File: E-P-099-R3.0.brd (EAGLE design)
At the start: 113.1 x 96.5 mm, 103 parts, among them J1 AVR_ISP, Q1 BSS101, Q2 BSS101, Q3 BSS101, Q4 BSS101, Q5 BSS101, Q6 BSS101

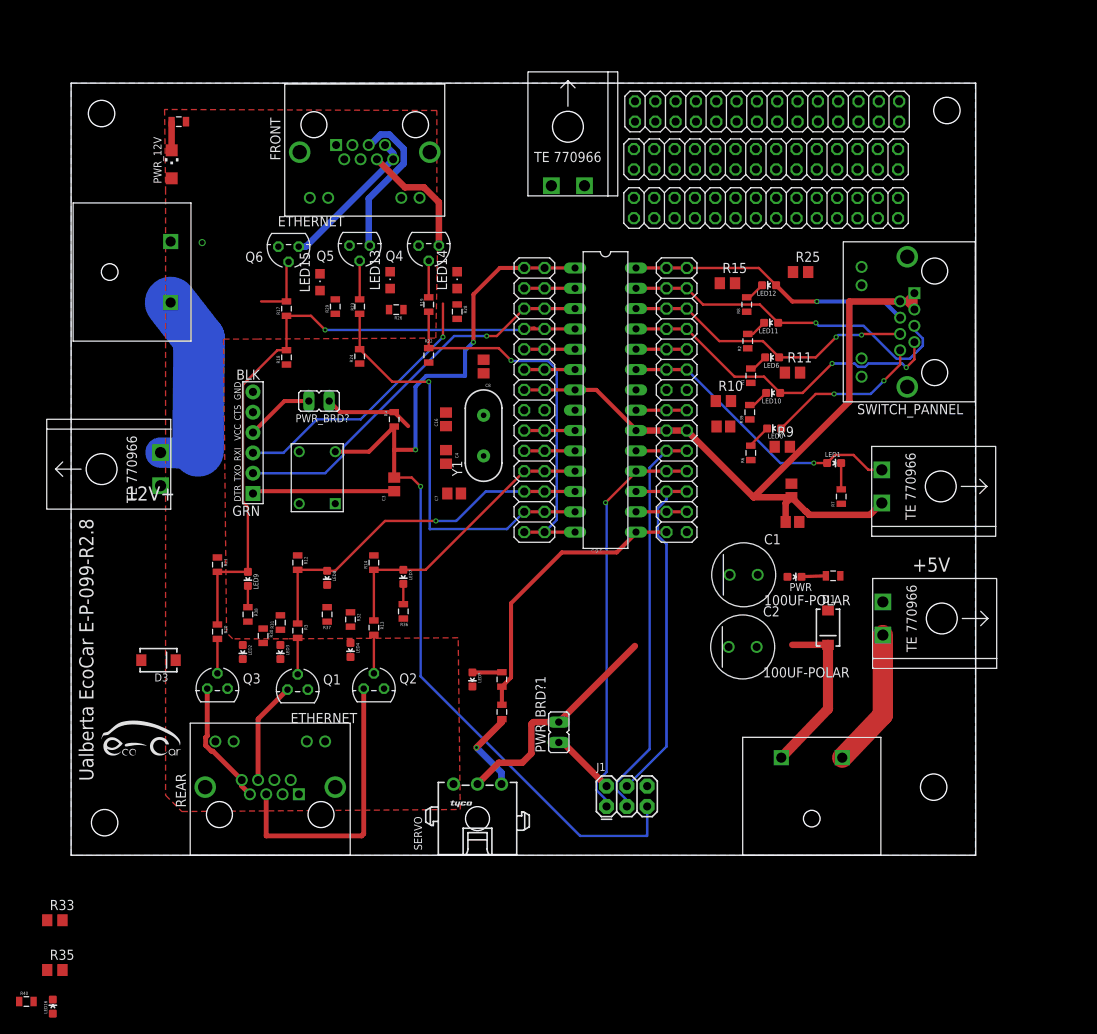
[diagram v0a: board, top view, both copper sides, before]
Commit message: added separate power for servo, cleaned up a bit of board layout, remade some missing eagle libraries and added them to library repo
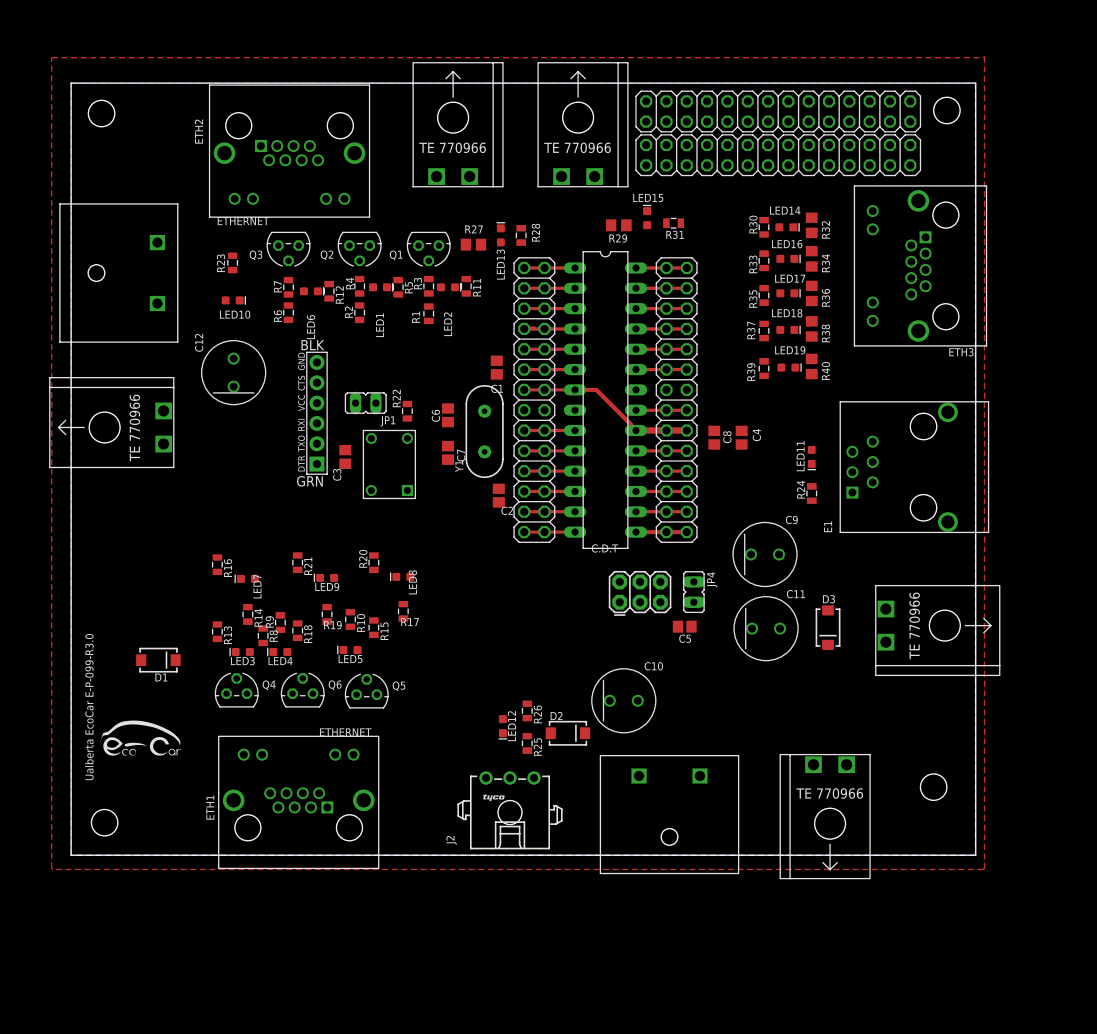
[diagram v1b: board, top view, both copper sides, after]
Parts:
- removed C14, C15, C16: 10uF, adafruit:C0805
- removed FRONT, REAR, SWITCH_PANNEL: ETHERNET, ETHERNET-3:A122645-ND
- removed LED0, PWR: (no value), SparkFun-LED:LED-0603
- removed PWR_12V: (no value), E14-P-099-R21.2(US_drills):CHIPLED_1206
- removed PWR_BRD?, PWR_BRD?1: (no value), E-P-099-R2.2:JP1
- removed SERVO: 1445055-3, con-amp:1445055-3
- removed U$1, U$3, U$5, U$8: TE770966, Shell2013(1):2X1-MATE-N-LOCK
- removed U$12: PUSH_BUTTON, E-P-099-R2.2:PUSHBUTTON
- removed U$2, U$9: FUSEMINI-BLADE, Shell2013:MINI-BLADE-FUSE
- removed U$4: ATMEGA328, E-P-099-R2.2:DIP28-0.3IN
- added AT1: ATMEGA328, atmega328p:DIP28-0.3IN
- added B1: PUSH_BUTTON, PushButton:PUSHBUTTON
- added C10, C11, C12, C9: 100UF-POLAR, 100uF_Cap:EEU-FR1H101
- added C6: 10uF, adafruit:C0805
- added D2: MBRA140, SparkFun-DiscreteSemi:SMA-DIODE
- added E1: 5555140-6, 5555140-6 RJ11:1734723-1_RJ11
- added ETH1, ETH2, ETH3: ETHERNET, ETHERNET-3:A122645-ND
- added J2: 1445055-3, con-amp:1445055-3
- added JP1: (no value), E-P-099-R2.2:JP1
- added LED17, LED18, LED19: (no value), SparkFun-LED:LED-0603
- added TE1, TE3: FUSEMINI-BLADE, Fuse:MINI-BLADE-FUSE
- added TE2, TE5, TE6, TE7: TE770966, TwoPinWhiteTEConnector:2X1-MATE-N-LOCK
- added TE4: SERVO_PWR, TwoPinWhiteTEConnector:2X1-MATE-N-LOCK
- C1, C2: value 100UF-POLAR -> 20pF; device 100uF_Cap:EEU-FR1H101 -> adafruit:C0805
- C4, C5: value 0.1uF -> 10uF
- C7, C8: value 20pF -> 0.1uF
- JP2: value (none) -> FTDI_DEVICE; device E-P-099-R2.2:2X14 -> SparkFun-Connectors:FTDI_DEVICE_SIDE
- JP4: device E-P-099-R2.2:2X14 -> E-P-099-R2.2:JP1
- JP6: value FTDI_DEVICE -> (none); device SparkFun-Connectors:FTDI_DEVICE_SIDE -> E-P-099-R2.2:2X14
- LED13, LED14, LED15: device led:CHIPLED_0805 -> SparkFun-LED:LED-0603
- R1, R2, R6: value 1K -> 10k
- R10, R9: value 10K -> 430; device resistor:R0805 -> SparkFun-Passives:0805
- R11, R33, R35: value 10K -> 1K; device resistor:R0805 -> SparkFun-Passives:0805
- R12, R22, R24: value 10k -> 1K
- R14: value 10k -> 430
- R15, R25: value 10K -> 100; device resistor:R0805 -> SparkFun-Passives:0805
- R16: value 1k -> 10k
- R17, R19: value 100 -> 430
- R18: value 10k -> 100
- R20: value 100 -> 10k
- R23: value 100 -> 1k
- R26, R8: value 1K -> 430
- R27: value 100 -> 10K; device SparkFun-Passives:0805 -> resistor:R0805
- R29, R40: value 1K -> 10K; device SparkFun-Passives:0805 -> resistor:R0805
- R30, R31, R37: value 430 -> 1K
- R32, R34, R36, R38: value 430 -> 10K; device SparkFun-Passives:0805 -> resistor:R0805
- R4, R7: value 1K -> 100
- moved LED16 131.0 mm to (78.1, 69.5)
- moved R40 126.2 mm to (81.2, 56.0), turned to 270 degrees
- moved R35 122.3 mm to (75.2, 64.9), turned to 270 degrees
- moved R33 121.0 mm to (75.2, 69.2), turned to 270 degrees
- moved D1 83.8 mm to (-0.51, 19.3), turned to 0 degrees
- moved D3 83.8 mm to (83.2, 23.4), turned to 270 degrees
- moved R30 80.8 mm to (75.2, 73.4), turned to 90 degrees
- moved R38 79.0 mm to (81.2, 60.7)
- moved JP6 77.6 mm to (77.0, 87.9), turned to 0 degrees
- moved R32 75.8 mm to (81.2, 73.7)
- moved R7 73.9 mm to (15.7, 65.9)
- moved R8 73.3 mm to (12.6, 22.4), turned to 270 degrees
- moved R31 70.0 mm to (63.9, 73.9), turned to 180 degrees
- moved LED10 68.5 mm to (8.76, 64.3), turned to 0 degrees
- moved R25 68.1 mm to (45.6, 8.89), turned to 270 degrees
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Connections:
- removed net N$24: C8.1, Y1.2
- new net N$29: TE3.IN, TE4.CIRCUIT1
- new net SERVO_V: C10.P, D2.C, J2.2, TE3.OUT
- net +12V: now also C12.P, D1.C, ETH1.P$1, ETH1.P$2, ETH1.P$3, ETH1.P$4, ETH2.P$1, ETH2.P$2, ETH2.P$3, ETH2.P$4, LED10.A, R10.1, R11.2, R12.1, R5.1, R8.1, R9.2, TE1.OUT; no longer D3.C, FRONT.P$1, FRONT.P$2, FRONT.P$3, FRONT.P$4, PWR_12V.A, R26.1, R28.2, R29.1, R30.1, R31.2, R32.1, REAR.P$1, REAR.P$2, REAR.P$3, REAR.P$4, U$9.OUT
- net +5V: now also AT1.20, AT1.7, C11.P, C6.1, C7.1, C8.1, C9.P, D3.C, ETH3.P$1, ETH3.P$2, ETH3.P$3, JP1.1, JP3.13, JP3.14, JP4.2, JP5.17, JP5.18, LED11.A, R22.2, TE5.CIRCUIT1, TE6.CIRCUIT1, TE7.CIRCUIT2; no longer C1.P, C14.1, C15.1, C16.1, C2.P, D1.C, JP3.17, JP3.18, JP4.13, JP4.14, PWR.A, PWR_BRD?.1, PWR_BRD?1.2, R4.2, SERVO.2, SWITCH_PANNEL.P$1, SWITCH_PANNEL.P$2, SWITCH_PANNEL.P$3, U$2.OUT, U$3.CIRCUIT1, U$4.20, U$4.7, U$5.CIRCUIT1
- net BLINK_L: now also AT1.13, JP3.25, JP3.26, R2.2, R4.2; no longer JP4.25, JP4.26, R23.2, R24.2, U$4.13
- net BLINK_R: now also AT1.14, JP3.27, JP3.28, R1.1, R3.2; no longer JP4.27, JP4.28, R19.2, R22.1, U$4.14
- net BREAK_SWITCH: now also AT1.23, JP5.11, JP5.12, LED13.A, R27.2, TE5.CIRCUIT2; no longer JP3.11, JP3.12, LED1.A, R35.2, U$3.CIRCUIT2, U$4.23
- net BRK_L_HIGH: now also AT1.12, JP3.23, JP3.24, LED9.A, R18.1, R21.2; no longer JP4.23, JP4.24, LED8.A, R12.2, R3.1, U$4.12
- net BRK_R_HIGH: now also AT1.11, JP3.21, JP3.22, LED8.A, R15.1, R20.1; no longer JP4.21, JP4.22, LED7.A, R13.1, R14.1, U$4.11
- net DRIVING_LIGHTS: now also AT1.4, JP3.7, JP3.8, LED7.A, R13.1, R16.2, R6.2, R7.1; no longer JP4.7, JP4.8, LED9.A, R17.1, R18.2, R20.1, R21.2, U$4.4
- net DRIVING_LIGHTS_SWITCH: now also AT1.26, ETH3.P$6, JP5.5, JP5.6, LED17.A, R36.2; no longer JP3.5, JP3.6, LED6.A, R11.2, SWITCH_PANNEL.P$6, U$4.26
- net DTR: now also JP2.P$1; no longer JP6.P$1
- net FREE: now also ETH3.P$8, LED19.A, R40.2; no longer LED0.A, R9.2, SWITCH_PANNEL.P$8
- net GND: now also AT1.22, AT1.8, B1.L1, C1.2, C10.G, C11.G, C12.G, C2.2, C6.2, C9.G, D2.A, E1.1, E1.6, E1.SH1, E1.SH2, ETH1.P$13, ETH1.P$14, J2.3, JP2.P$6, JP3.15, JP3.16, JP5.13, JP5.14, LED12.C, R1.2, R16.1, R17.2, R19.2, R20.2, R23.2, R27.1, R28.1, R29.2, R30.1, R31.1, R32.1, R33.1, R34.1, R36.1, R37.1, R38.1, TE2.CIRCUIT2, TE4.CIRCUIT2; no longer C1.G, C14.2, C15.2, C16.2, C2.G, JP3.13, JP3.14, JP4.15, JP4.16, JP6.P$6, LED5.C, R1.1, R10.1, R11.1, R12.1, R15.1, R16.2, R18.1, R22.2, R25.1, R33.2, R36.2, R37.2, R38.2, R5.1, R7.1, R8.1, R9.1, REAR.P$13, REAR.P$14, SERVO.3, U$1.CIRCUIT2, U$12.L1, U$4.22, U$4.8, U$8.CIRCUIT2
- net HAZ_SWITCH: now also AT1.25, ETH3.P$7, JP5.7, JP5.8, LED18.A, R38.2; no longer JP3.7, JP3.8, LED10.A, R10.2, SWITCH_PANNEL.P$7, U$4.25
- net LEFT_SWITCH: now also AT1.27, ETH3.P$5, JP5.3, JP5.4, LED16.A, R34.2; no longer JP3.3, JP3.4, LED11.A, R15.2, SWITCH_PANNEL.P$5, U$4.27
- net MISO: now also AT1.18, JP5.21, JP5.22; no longer JP3.21, JP3.22, U$4.18
- net MOSI: now also AT1.17, JP5.23, JP5.24; no longer JP3.23, JP3.24, U$4.17
- net N$1: now also LED14.C, R30.2; no longer LED12.C, R8.2
- net N$10: now also LED19.C, R39.2; no longer LED0.C, R6.2
- net N$11: now also LED13.C, R28.2; no longer LED1.C, R7.2
- net N$12: now also LED12.A, R26.1; no longer LED5.A, R34.1
- net N$13: now also J2.1, R25.2; no longer R27.2, SERVO.1
- net N$14: now also Q5.2, R15.2; no longer Q2.2, R13.2
- net N$15: now also Q6.2, R18.2; no longer Q1.2, R3.2
- net N$16: now also LED10.C, R23.1; no longer PWR_12V.C, R16.1
- net N$17: now also Q2.2, R4.1; no longer Q5.2, R23.1
- net N$18: now also LED5.A, R10.2; no longer LED4.A, R32.2
- net N$19: now also LED11.C, R24.2; no longer PWR.C, R5.2
- net N$2: now also LED17.C, R35.2; no longer LED6.C, R1.2
- net N$20: now also ETH2.P$7, ETH2.P$8, LED6.C, Q3.3; no longer FRONT.P$7, FRONT.P$8, LED15.C, Q6.3
- net N$21: now also ETH2.P$6, LED2.C, Q1.3; no longer FRONT.P$6, LED14.C, Q4.3
- net N$22: now also ETH2.P$5, LED1.C, Q2.3; no longer FRONT.P$5, LED13.C, Q5.3
- net N$23: now also LED4.A, R9.1; no longer LED3.A, R31.1
- net N$25: now also AT1.6, JP3.11, JP3.12; no longer JP4.11, JP4.12, U$4.6
- net N$26: now also AT1.5, JP3.10, JP3.9; no longer JP4.10, JP4.9, U$4.5
- net N$27: now also LED3.A, R8.2; no longer LED2.A, R30.2
- net N$28: now also LED15.C, R31.2; no longer LED16.C, R40.2
- net N$3: now also LED16.C, R33.2; no longer LED11.C, R2.2
- net N$32: now also LED1.A, R5.2; no longer LED13.A, R26.2
- net N$33: now also Q1.2, R3.1; no longer Q4.2, R19.1
- net N$34: now also LED2.A, R11.1; no longer LED14.A, R28.1
- net N$35: now also Q3.2, R7.2; no longer Q6.2, R17.2
- net N$36: now also LED6.A, R12.2; no longer LED15.A, R29.2
- net N$37: now also JP4.1; no longer PWR_BRD?1.1
- net N$4: now also ETH1.P$7, ETH1.P$8, LED3.C, Q4.3; no longer LED2.C, Q3.3, REAR.P$7, REAR.P$8
- net N$41: now also LED8.C, R17.1; no longer LED7.C, R36.1
- net N$42: now also LED9.C, R19.1; no longer LED8.C, R37.1
- net N$44: now also LED7.C, R14.1; no longer LED9.C, R38.1
- net N$46: now also LED18.C, R37.2; no longer LED10.C, R39.2
- net N$47: now also TE1.IN, TE2.CIRCUIT1; no longer U$8.CIRCUIT1, U$9.IN
- net N$5: now also ETH1.P$6, LED4.C, Q6.3; no longer LED3.C, Q1.3, REAR.P$6
- net N$6: now also E1.3, E1.4, TE7.CIRCUIT1; no longer U$1.CIRCUIT1, U$2.IN
- net N$60: now also AT1.21, JP5.15, JP5.16; no longer JP3.15, JP3.16, U$4.21
- net N$65: now also AT1.16, JP5.25, JP5.26; no longer JP3.25, JP3.26, U$4.16
- net N$7: now also ETH1.P$5, LED5.C, Q5.3; no longer LED4.C, Q2.3, REAR.P$5
- net N$8: now also Q4.2, R13.2; no longer Q3.2, R20.2
- net N$9: now also JP1.2, JP2.P$4; no longer JP6.P$4, PWR_BRD?.2
- net RESET: now also AT1.1, B1.R2, JP3.1, JP3.2, R22.1; no longer JP4.1, JP4.2, R4.1, U$12.R2, U$4.1
- net RIGHT_SWITCH: now also AT1.28, ETH3.P$4, JP5.1, JP5.2, LED14.A, R32.2; no longer JP3.1, JP3.2, LED12.A, R25.2, SWITCH_PANNEL.P$4, U$4.28
- net RX: now also AT1.2, JP2.P$3, JP3.3, JP3.4; no longer JP4.3, JP4.4, JP6.P$3, U$4.2
- net SCK: now also AT1.19, JP5.19, JP5.20; no longer JP3.19, JP3.20, U$4.19
- net SERVO: now also AT1.15, JP5.27, JP5.28, R25.1, R26.2; no longer JP3.27, JP3.28, R27.1, R34.2, U$4.15
- net TX: now also AT1.3, JP2.P$2, JP3.5, JP3.6; no longer JP4.5, JP4.6, JP6.P$2, U$4.3
- net WIPER_SWITCH: now also AT1.24, JP5.10, JP5.9, LED15.A, R29.1, TE6.CIRCUIT2; no longer JP3.10, JP3.9, LED16.A, R33.1, U$4.24, U$5.CIRCUIT2
- net XTAL1: now also AT1.9, C1.1, JP3.17, JP3.18, Y1.2; no longer JP4.17, JP4.18, U$4.9
- net XTAL2: now also AT1.10, C2.1, JP3.19, JP3.20; no longer C7.1, JP4.19, JP4.20, U$4.10
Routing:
- net +5V: track 160.8 -> 23.7 mm
- net RESET: track 125.5 -> 6.35 mm, vias 3 -> 0
- net DRIVING_LIGHTS: track 83.7 -> 7.81 mm, vias 1 -> 0
- net SCK: track 53.9 -> 6.35 mm
- net BLINK_L: track 52.3 -> 6.35 mm, vias 1 -> 0
- net MISO: track 52.0 -> 6.48 mm, vias 1 -> 0
- net TX: track 49.4 -> 6.35 mm, vias 1 -> 0
- net BLINK_R: track 49.4 -> 6.79 mm, vias 1 -> 0
- net MOSI: track 46.1 -> 6.35 mm
- net BRK_L_HIGH: track 45.5 -> 6.35 mm, vias 1 -> 0
- net LEFT_SWITCH: track 43.1 -> 6.35 mm, vias 1 -> 0
- net HAZ_SWITCH: track 42.8 -> 6.35 mm, vias 2 -> 0
- net N$7: track 35.7 -> 0.00 mm
- net RX: track 40.5 -> 6.53 mm, vias 1 -> 0
- net BREAK_SWITCH: track 36.8 -> 6.35 mm, vias 1 -> 0
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- added copper zone on layer 1, net GND
- removed copper zone on layer 1, net +12V
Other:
- board text added: "Ualberta EcoCar E-P-099-R3.0"
- board text removed: "+5V"
- board text removed: "12V+"
- board text removed: "Ualberta EcoCar E-P-099-R2.8"

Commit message: added silk screen labels to some parts. moved back to coordinate system origin
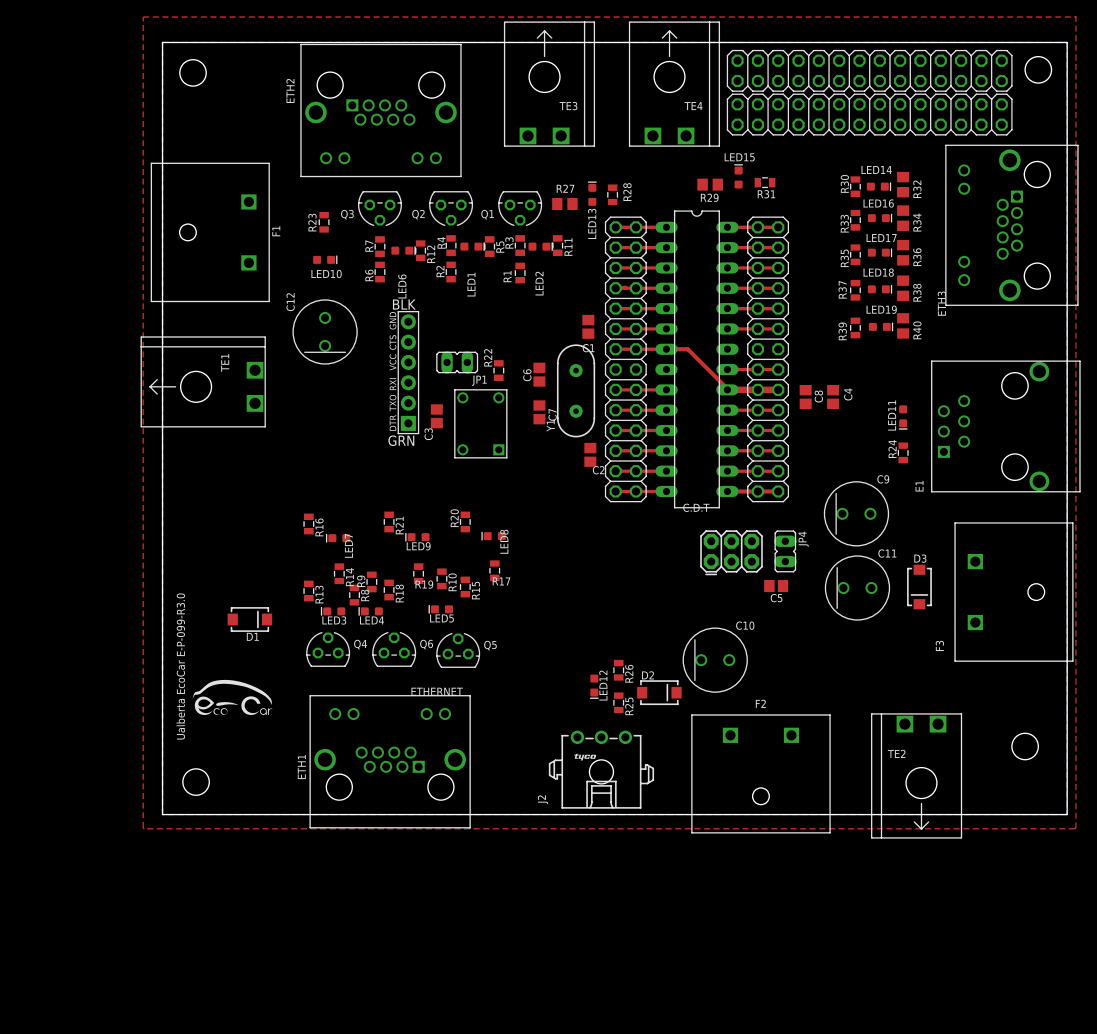
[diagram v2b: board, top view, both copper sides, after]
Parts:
- removed TE5, TE6, TE7: TE770966, TwoPinWhiteTEConnector:2X1-MATE-N-LOCK
- added F1, F2, F3: FUSEMINI-BLADE, Fuse:MINI-BLADE-FUSE
- TE1, TE3: value FUSEMINI-BLADE -> TE770966; device Fuse:MINI-BLADE-FUSE -> TwoPinWhiteTEConnector:2X1-MATE-N-LOCK
- TE2: value TE770966 -> SERVO_PWR
- TE4: value SERVO_PWR -> TE770966
- moved TE2 120.4 mm to (94.9, -2.92), turned to 0 degrees
- moved TE4 108.9 mm to (63.4, 99.1), turned to 180 degrees
- moved TE3 103.0 mm to (47.8, 99.1), turned to 180 degrees
- moved TE1 15.3 mm to (-2.67, 53.5)
- moved C8 12.5 mm to (80.4, 52.2)
- moved AT1 12.5 mm to (66.8, 56.9)
- moved E1 12.5 mm to (100.2, 49.1)
- moved LED14 12.5 mm to (89.4, 78.5)
- moved LED19 12.5 mm to (89.7, 61.0)
- moved R30 12.5 mm to (86.6, 78.5)
- moved R31 12.5 mm to (75.3, 79.0)
- moved R33 12.5 mm to (86.6, 74.3)
- moved R35 12.5 mm to (86.6, 70.0)
- moved R37 12.5 mm to (86.6, 65.5)
- moved R39 12.5 mm to (86.6, 60.8)
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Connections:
- removed net N$65: AT1.16, JP5.25, JP5.26
- net +12V: now also F1.OUT; no longer TE1.OUT
- net +5V: now also F3.OUT, TE3.CIRCUIT1, TE4.CIRCUIT1; no longer TE5.CIRCUIT1, TE6.CIRCUIT1, TE7.CIRCUIT2
- net BREAK_SWITCH: now also TE3.CIRCUIT2; no longer TE5.CIRCUIT2
- net FREE: now also AT1.16, JP5.25, JP5.26
- net GND: now also TE1.CIRCUIT2; no longer TE4.CIRCUIT2
- net N$29: now also F2.IN, TE2.CIRCUIT1; no longer TE3.IN, TE4.CIRCUIT1
- net N$47: now also F1.IN, TE1.CIRCUIT1; no longer TE1.IN, TE2.CIRCUIT1
- net N$6: now also F3.IN; no longer TE7.CIRCUIT1
- net SERVO_V: now also F2.OUT; no longer TE3.OUT
- net WIPER_SWITCH: now also TE4.CIRCUIT2; no longer TE6.CIRCUIT2
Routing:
- net FREE: track 0.00 -> 6.35 mm
- net N$65: track 6.35 -> 0.00 mm

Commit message: took some signals off of steering wheel and put on new ethernet
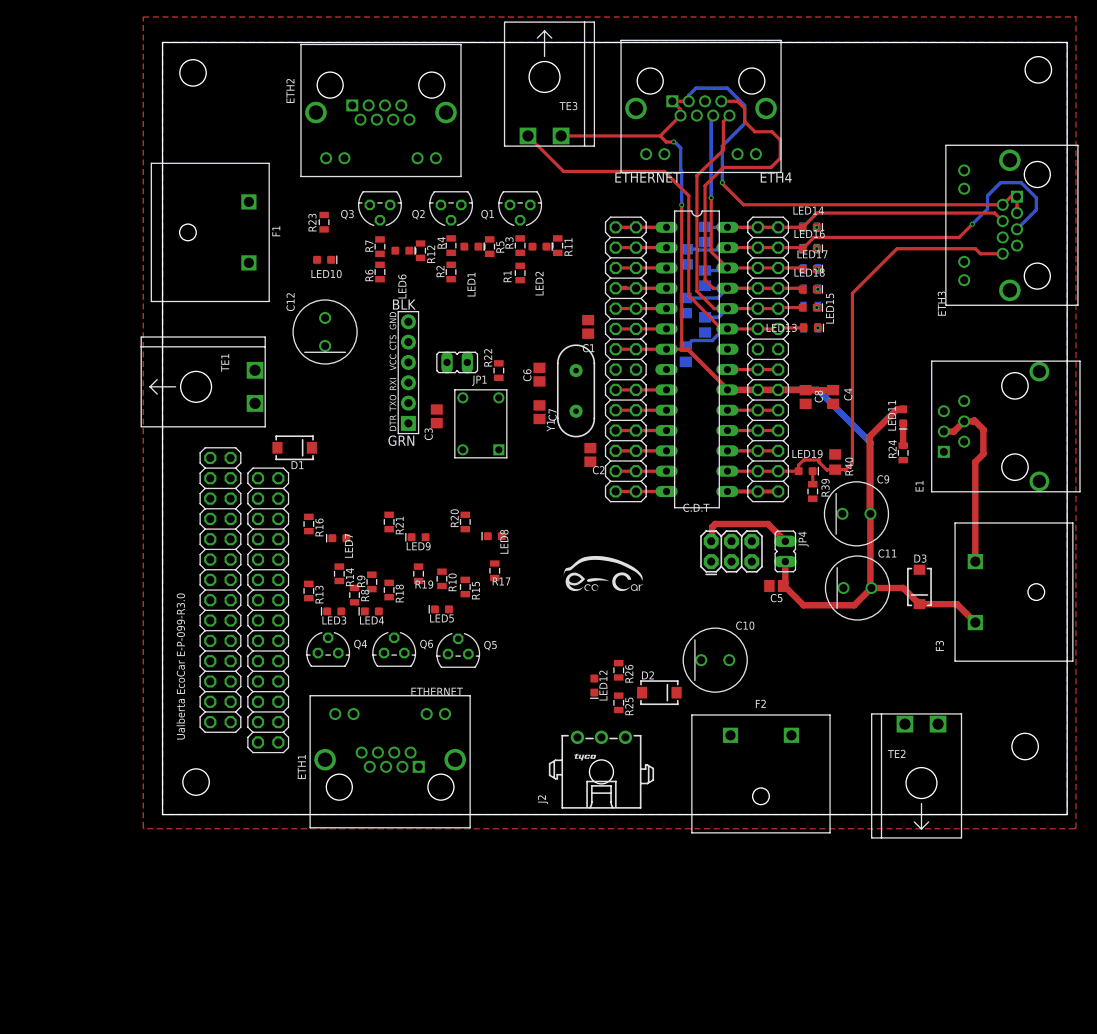
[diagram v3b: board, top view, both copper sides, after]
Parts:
- removed TE4: TE770966, TwoPinWhiteTEConnector:2X1-MATE-N-LOCK
- added ETH4: ETHERNET, ETHERNET-3:A122645-ND
- moved JP6 101.0 mm to (13.2, 25.5), turned to 90 degrees
- moved JP7 100.6 mm to (7.24, 28.1), turned to 90 degrees
- moved LED13 32.0 mm to (81.0, 60.8), turned to 0 degrees
- moved R28 29.8 mm to (81.0, 60.8), flipped to the bottom, turned to 180 degrees
- moved R34 27.5 mm to (65.5, 69.7), flipped to the bottom, turned to 90 degrees
- moved R38 27.3 mm to (65.4, 63.6), flipped to the bottom, turned to 90 degrees
- moved R32 25.5 mm to (67.8, 72.5), flipped to the bottom, turned to 90 degrees
- moved R36 25.0 mm to (67.8, 67.1), flipped to the bottom, turned to 90 degrees
- moved R27 24.1 mm to (65.4, 57.5), flipped to the bottom, turned to 90 degrees
- moved D1 22.2 mm to (16.5, 45.8)
- moved R39 21.1 mm to (81.3, 40.4), turned to 90 degrees
- moved LED19 20.3 mm to (80.4, 42.9)
- moved R40 19.0 mm to (84.1, 44.1)
- moved LED15 18.5 mm to (80.9, 63.4), turned to 0 degrees
- moved R29 17.5 mm to (67.8, 61.2), flipped to the bottom, turned to 90 degrees
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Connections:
- net +5V: now also ETH4.P$1, ETH4.P$2, ETH4.P$3; no longer TE4.CIRCUIT1
- net DRIVING_LIGHTS_SWITCH: now also ETH4.P$6; no longer ETH3.P$6
- net GND: now also ETH3.P$13, ETH3.P$14, ETH4.P$13, ETH4.P$14, R29.1, R31.2; no longer R29.2, R31.1
- net HAZ_SWITCH: now also ETH4.P$7; no longer ETH3.P$7
- net N$28: now also R31.1; no longer R31.2
- net WIPER_SWITCH: now also ETH4.P$8, R29.2; no longer R29.1, TE4.CIRCUIT2
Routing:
- net +5V: track 23.7 -> 218.2 mm, vias 0 -> 3
- net FREE: track 6.35 -> 60.3 mm
- net BREAK_SWITCH: track 6.35 -> 58.2 mm
- net LEFT_SWITCH: track 6.35 -> 54.0 mm, vias 0 -> 1
- net HAZ_SWITCH: track 6.35 -> 53.6 mm
- net WIPER_SWITCH: track 6.35 -> 41.1 mm
- net RIGHT_SWITCH: track 6.35 -> 38.4 mm
- net DRIVING_LIGHTS_SWITCH: track 6.35 -> 32.4 mm, vias 0 -> 1
- net N$6: track 0.00 -> 22.9 mm
- net N$37: track 0.00 -> 12.0 mm
- net N$19: track 0.00 -> 2.79 mm
- net N$10: track 0.00 -> 1.64 mm
- net N$28: track 0.00 -> 0.20 mm, vias 0 -> 1
- net N$46: track 0.00 -> 0.15 mm, vias 0 -> 1
- net N$2: track 0.00 -> 0.15 mm, vias 0 -> 1
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
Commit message: update
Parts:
- removed LED7, LED8, LED9: (no value), SparkFun-LED:LED-0603
- removed R14, R17, R19: 430, SparkFun-Passives:0805
- moved D1 31.2 mm to (16.4, 77.1), turned to 90 degrees
- moved R8 7.47 mm to (17.9, 31.8)
- moved R16 5.34 mm to (20.8, 31.6)
- moved R21 5.11 mm to (28.8, 31.5)
- moved R20 5.03 mm to (37.0, 31.6)
- moved LED3 4.45 mm to (17.9, 28.1), turned to 270 degrees
- moved R13 2.54 mm to (20.8, 27.9)
- moved LED4 2.29 mm to (26.2, 27.7), turned to 270 degrees
- moved R9 2.29 mm to (26.2, 31.4)
- moved R10 2.25 mm to (34.3, 31.6)
- moved LED5 2.01 mm to (34.3, 27.6), turned to 270 degrees
- moved R15 1.44 mm to (36.8, 27.4)
- moved D2 0.77 mm to (62.2, 14.5)
- moved R18 0.72 mm to (28.8, 27.6)
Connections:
- removed net N$41: LED8.C, R17.1
- removed net N$42: LED9.C, R19.1
- removed net N$44: LED7.C, R14.1
- net BRK_L_HIGH: no longer LED9.A
- net BRK_R_HIGH: no longer LED8.A
- net DRIVING_LIGHTS: no longer LED7.A
- net GND: no longer R14.2, R17.2, R19.2
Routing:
- net +12V: track 0.00 -> 205.7 mm, vias 0 -> 2
- net RESET: track 6.35 -> 103.4 mm
- net DRIVING_LIGHTS: track 7.81 -> 88.3 mm, vias 0 -> 4
- net BLINK_L: track 6.35 -> 48.9 mm, vias 0 -> 2
- net N$7: track 0.00 -> 41.1 mm, vias 0 -> 1
- net BLINK_R: track 6.79 -> 45.9 mm
- net SERVO_V: track 0.00 -> 36.6 mm
- net BRK_L_HIGH: track 6.35 -> 42.5 mm, vias 0 -> 3
- net TX: track 6.35 -> 42.5 mm, vias 0 -> 1
- net RX: track 6.53 -> 41.7 mm, vias 0 -> 1
- net SERVO: track 6.35 -> 41.1 mm, vias 0 -> 1
- net SCK: track 6.35 -> 40.6 mm
- net BRK_R_HIGH: track 6.35 -> 37.6 mm, vias 0 -> 1
- net N$21: track 0.00 -> 28.3 mm
- net N$22: track 0.00 -> 27.2 mm
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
